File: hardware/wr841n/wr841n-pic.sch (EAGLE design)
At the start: 40 parts, among them IC1 PIC18F26K80, IC2 ISO1050, IC3 ADUM1251, IC4 ADUM1201, IC5 ADUM1201

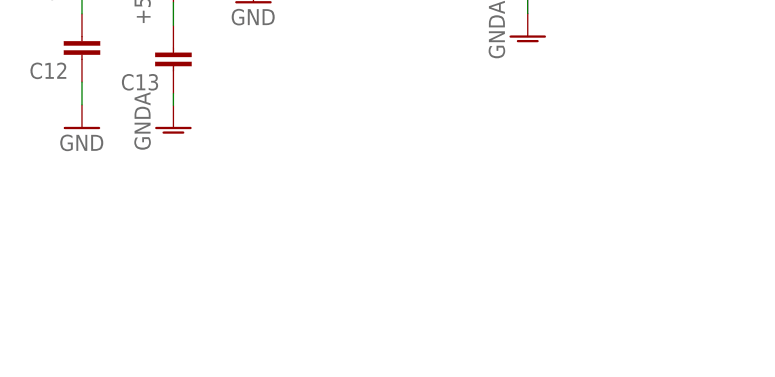
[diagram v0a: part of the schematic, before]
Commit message: add license
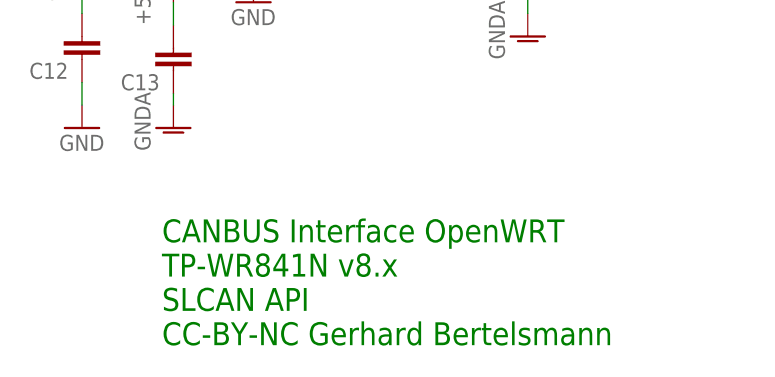
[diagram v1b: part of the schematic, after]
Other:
- note added: "CANBUS Interface OpenWRT TP-WR841N v8.x SLCAN API CC-BY-NC Gerhard Bertelsmann"
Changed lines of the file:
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@@
 <part name="GND24" library="supply1" deviceset="GND" device=""/>
 <part name="GND25" library="supply1" deviceset="GND" device=""/>
+<part name="FRAME1" library="frames" deviceset="A4L-LOC" device=""/>
 </parts>
 <sheets>
 <sheet>
 <plain>
+<text x="106.68" y="-33.02" size="2.54" layer="91">CANBUS Interface OpenWRT
+TP-WR841N v8.x
+SLCAN API
+CC-BY-NC Gerhard Bertelsmann</text>
 </plain>
 <instances>
@@
 <instance part="GND24" gate="1" x="-7.62" y="20.32"/>
 <instance part="GND25" gate="1" x="0" y="20.32"/>
+<instance part="FRAME1" gate="G$1" x="-58.42" y="-40.64"/>
 </instances>
 <busses>
@@
 </schematic>
 </drawing>
+<compatibility>
+<note version="6.3" minversion="6.2.2" severity="warning">
+Since Version 6.2.2 text objects can contain more than one line,
+which will not be processed correctly with this version.
+</note>
+</compatibility>
 </eagle>
